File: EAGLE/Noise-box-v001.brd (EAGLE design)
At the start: 160 x 100 mm, 29 parts, among them J1 AVR_SPI_PROG_3X22X3_LOCK, J2 BATT, J4 MICRO-SD_CARD_SOCKET, J5 AUDIO_JACK_3.5MM_SMD, U1 ATMEGA328P_TQFP, U2 MIC5219 3.3V, U3 MCP73831, Y1 12.288MHz

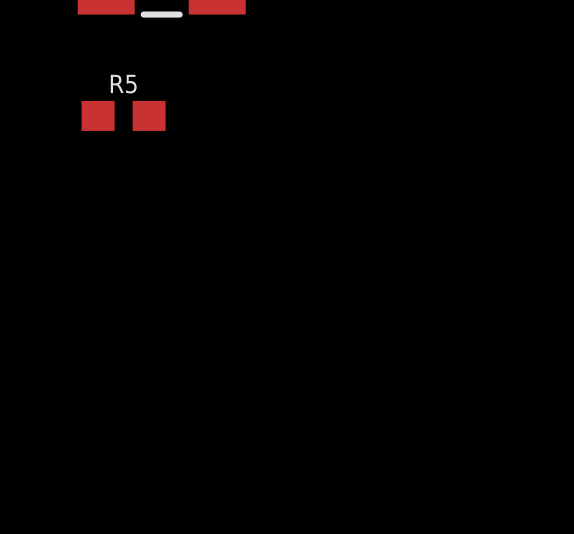
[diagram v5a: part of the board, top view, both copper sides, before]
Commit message: clk
Added crystal for vs1063
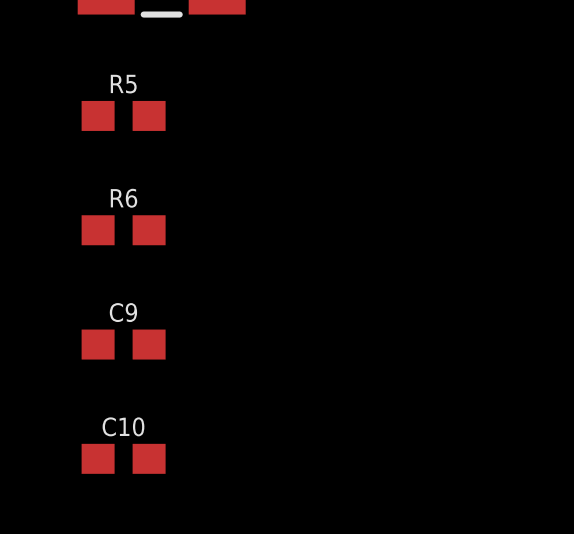
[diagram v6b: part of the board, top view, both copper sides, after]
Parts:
- added C10, C9: 22pF, SparkFun-Capacitors:0603
- added R6: 1M, SparkFun-Resistors:0603
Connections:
- new net N$10: U$3.23
- new net N$11: U$3.13
- new net N$12: U$3.8
- new net N$13: U$3.3
- new net N$14: U$3.32
- new net N$17: C9.2, R6.2, U$3.18, Y1.3
- new net N$18: C10.2, R6.1, U$3.17, Y1.1
- new net N$7: U$3.30
- new net N$8: U$3.29
- new net N$9: U$3.28
- net GND: now also C10.1, C9.1
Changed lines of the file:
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@@
 <attribute name="PROD_ID" value="RES-07828" x="-49.53" y="-134.62" size="1.778" layer="27" display="off"/>
+</element>
+<element name="R6" library="SparkFun-Resistors" package="0603" value="1M" x="-49.53" y="-138.43">
+<attribute name="PROD_ID" value="RES-07868" x="-49.53" y="-138.43" size="1.778" layer="27" display="off"/>
+</element>
+<element name="C9" library="SparkFun-Capacitors" package="0603" value="22pF" x="-49.53" y="-142.24">
+<attribute name="PROD_ID" value="CAP-07876" x="-49.53" y="-142.24" size="1.778" layer="27" display="off"/>
+</element>
+<element name="C10" library="SparkFun-Capacitors" package="0603" value="22pF" x="-49.53" y="-146.05">
+<attribute name="PROD_ID" value="CAP-07876" x="-49.53" y="-146.05" size="1.778" layer="27" display="off"/>
 </element>
 </elements>
@@
 <contactref element="U$3" pad="47"/>
 <contactref element="R5" pad="1"/>
+<contactref element="C9" pad="1"/>
+<contactref element="C10" pad="1"/>
+<wire x1="-50.38" y1="-142.24" x2="-50.38" y2="-146.05" width="0" layer="19" extent="1-1"/>
+<wire x1="-50.38" y1="-134.62" x2="-50.38" y2="-142.24" width="0" layer="19" extent="1-1"/>
 <wire x1="-45.7" y1="-124.9" x2="-50.38" y2="-134.62" width="0" layer="19" extent="1-1"/>
 <wire x1="-48.7" y1="-122.9" x2="-45.7" y2="-124.9" width="0" layer="19" extent="1-1"/>
@@
 <wire x1="-41.7" y1="-124.9" x2="-42.2" y2="-124.9" width="0" layer="19" extent="1-1"/>
 </signal>
+<signal name="N$7">
+<contactref element="U$3" pad="30"/>
+</signal>
+<signal name="N$8">
+<contactref element="U$3" pad="29"/>
+</signal>
+<signal name="N$9">
+<contactref element="U$3" pad="28"/>
+</signal>
+<signal name="N$10">
+<contactref element="U$3" pad="23"/>
+</signal>
+<signal name="N$11">
+<contactref element="U$3" pad="13"/>
+</signal>
+<signal name="N$12">
+<contactref element="U$3" pad="8"/>
+</signal>
+<signal name="N$13">
+<contactref element="U$3" pad="3"/>
+</signal>
+<signal name="N$14">
+<contactref element="U$3" pad="32"/>
+</signal>
+<signal name="N$17">
+<contactref element="U$3" pad="18"/>
+<contactref element="Y1" pad="3"/>
+<contactref element="C9" pad="2"/>
+<contactref element="R6" pad="2"/>
+<wire x1="-48.68" y1="-138.43" x2="-48.68" y2="-142.24" width="0" layer="19" extent="1-1"/>
+<wire x1="-46.41" y1="-128.39" x2="-48.68" y2="-138.43" width="0" layer="19" extent="1-1"/>
+<wire x1="-40.2" y1="-120.9" x2="-46.41" y2="-128.39" width="0" layer="19" extent="1-1"/>
+</signal>
+<signal name="N$18">
+<contactref element="U$3" pad="17"/>
+<contactref element="C10" pad="2"/>
+<contactref element="Y1" pad="1"/>
+<contactref element="R6" pad="1"/>
+<wire x1="-50.38" y1="-138.43" x2="-48.68" y2="-146.05" width="0" layer="19" extent="1-1"/>
+<wire x1="-50.11" y1="-130.69" x2="-50.38" y2="-138.43" width="0" layer="19" extent="1-1"/>
+<wire x1="-40.2" y1="-121.4" x2="-50.11" y2="-130.69" width="0" layer="19" extent="1-1"/>
+</signal>
 </signals>

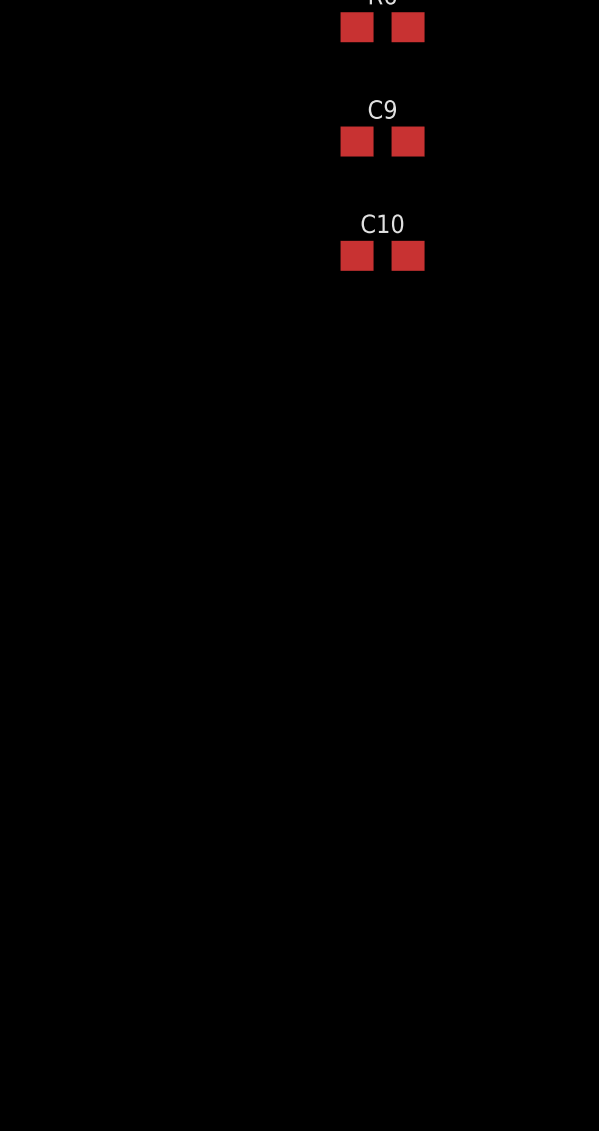
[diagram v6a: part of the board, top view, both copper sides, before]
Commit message: vs1063
Added all support circuitry to vs1063, including extra locations for cap
filtering
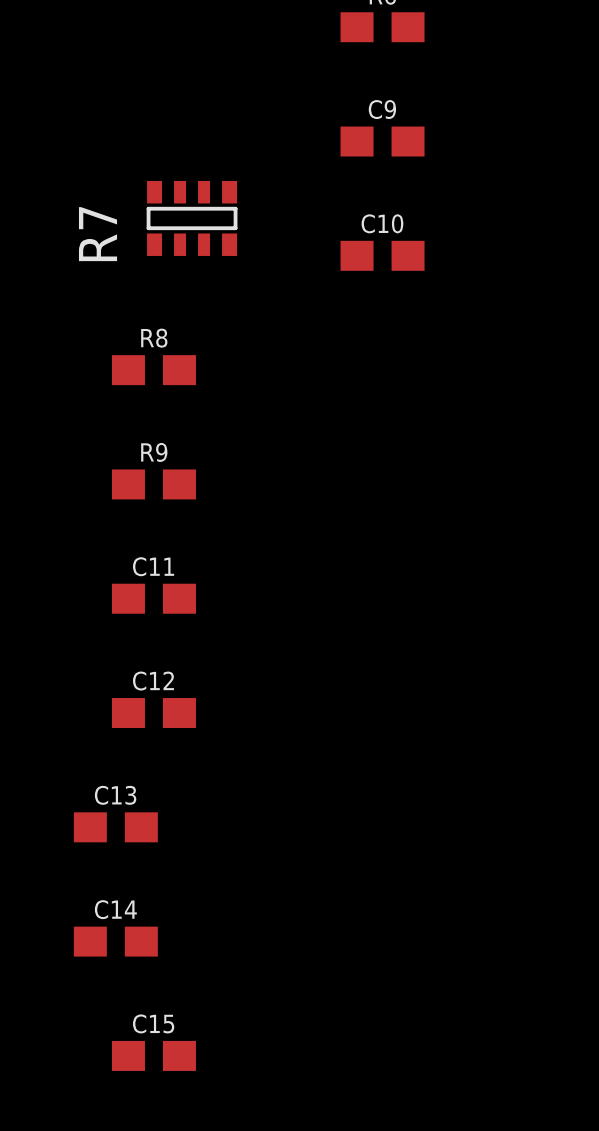
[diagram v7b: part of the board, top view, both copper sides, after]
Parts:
- added C11, C13, C14, C15: 0.1uF, SparkFun-Capacitors:0603
- added C12: 1.0uF, SparkFun-Capacitors:0603
- added R7: RN-4_100K, RJC-2:MNR14
- added R8, R9: 100k, SparkFun-Resistors:0603
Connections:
- net N$10 renamed MP3-CS
- net N$11 renamed MP3-DCS
- net N$12 renamed MP3-DREQ
- removed net N$13: U$3.3
- removed net N$7: U$3.30
- removed net N$8: U$3.29
- removed net N$9: U$3.28
- new net EN-GPIO1: R7.6, U$3.34
- new net GBUF: U$3.42
- new net GPIO0: R7.5, U$3.33
- new net LEFT: U$3.46
- new net MP3-MIDI-RX: R9.1, U$3.26
- new net MP3-RST: R8.1, U$3.3
- new net N$15: R7.7, U$3.36
- new net N$21: C12.1, U$3.44
- new net RIGHT: U$3.39
- net +3V3: now also C11.1, C13.1, C14.1, R8.2, R9.2, U$3.14, U$3.19, U$3.32, U$3.38, U$3.43, U$3.45, U$3.6
- net GND: now also C11.2, C12.2, C13.2, C14.2, C15.2, R7.1, R7.2, R7.3, R7.4
- net MISO: now also U$3.30
- net MOSI: now also U$3.29
- net N$14: now also R7.8, U$3.25; no longer U$3.32
- net SCK: now also U$3.28
- net VCC: now also C15.1, U$3.24, U$3.31, U$3.5, U$3.7
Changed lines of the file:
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@@
 <layer number="230" name="230bmp" color="7" fill="1" visible="yes" active="yes"/>
 <layer number="231" name="231bmp" color="7" fill="1" visible="yes" active="yes"/>
+<layer number="232" name="Eagle3D_PG2" color="7" fill="1" visible="no" active="no"/>
+<layer number="233" name="Eagle3D_PG3" color="7" fill="1" visible="no" active="no"/>
 <layer number="248" name="Housing" color="7" fill="1" visible="yes" active="yes"/>
 <layer number="249" name="Edge" color="7" fill="1" visible="yes" active="yes"/>
@@
 <attribute name="PROD_ID" value="CAP-07876" x="-49.53" y="-146.05" size="1.778" layer="27" display="off"/>
 </element>
+<element name="R7" library="RJC-2" package="MNR14" value="RN-4_100K" x="-55.88" y="-144.78">
+<attribute name="PARTNO" value="MNR14ERAPJ104" x="-55.88" y="-144.78" size="1.778" layer="27" display="off"/>
+</element>
+<element name="R8" library="SparkFun-Resistors" package="0603" value="100k" x="-57.15" y="-149.86">
+<attribute name="PROD_ID" value="RES-07828" x="-57.15" y="-149.86" size="1.778" layer="27" display="off"/>
+</element>
+<element name="R9" library="SparkFun-Resistors" package="0603" value="100k" x="-57.15" y="-153.67">
+<attribute name="PROD_ID" value="RES-07828" x="-57.15" y="-153.67" size="1.778" layer="27" display="off"/>
+</element>
+<element name="C11" library="SparkFun-Capacitors" package="0603" value="0.1uF" x="-57.15" y="-157.48">
+<attribute name="PROD_ID" value="CAP-08604" x="-57.15" y="-157.48" size="1.778" layer="27" display="off"/>
+</element>
+<element name="C12" library="SparkFun-Capacitors" package="0603" value="1.0uF" x="-57.15" y="-161.29">
+<attribute name="PROD_ID" value="CAP-00868" x="-57.15" y="-161.29" size="1.778" layer="27" display="off"/>
+</element>
+<element name="C13" library="SparkFun-Capacitors" package="0603" value="0.1uF" x="-58.42" y="-165.1">
+<attribute name="PROD_ID" value="CAP-08604" x="-57.15" y="-165.1" size="1.778" layer="27" display="off"/>
+</element>
+<element name="C14" library="SparkFun-Capacitors" package="0603" value="0.1uF" x="-58.42" y="-168.91">
+<attribute name="PROD_ID" value="CAP-08604" x="-57.15" y="-168.91" size="1.778" layer="27" display="off"/>
+</element>
+<element name="C15" library="SparkFun-Capacitors" package="0603" value="0.1uF" x="-57.15" y="-172.72">
+<attribute name="PROD_ID" value="CAP-08604" x="-57.15" y="-172.72" size="1.778" layer="27" display="off"/>
+</element>
 </elements>
 <signals>
@@
 <contactref element="U$1" pad="3"/>
 <contactref element="J4" pad="VCC"/>
+<contactref element="U$3" pad="38"/>
+<contactref element="U$3" pad="45"/>
+<contactref element="U$3" pad="43"/>
+<contactref element="U$3" pad="6"/>
+<contactref element="U$3" pad="19"/>
+<contactref element="U$3" pad="14"/>
+<contactref element="U$3" pad="32"/>
+<contactref element="R9" pad="2"/>
+<contactref element="R8" pad="2"/>
+<contactref element="C11" pad="1"/>
+<contactref element="C13" pad="1"/>
+<contactref element="C14" pad="1"/>
+<wire x1="-59.27" y1="-165.1" x2="-59.27" y2="-168.91" width="0" layer="19" extent="1-1"/>
+<wire x1="-58" y1="-157.48" x2="-59.27" y2="-165.1" width="0" layer="19" extent="1-1"/>
+<wire x1="-56.3" y1="-153.67" x2="-58" y2="-157.48" width="0" layer="19" extent="1-1"/>
+<wire x1="-56.3" y1="-149.86" x2="-56.3" y2="-153.67" width="0" layer="19" extent="1-1"/>
+<wire x1="-44.7" y1="-124.9" x2="-56.3" y2="-149.86" width="0" layer="19" extent="1-1"/>
+<wire x1="-40.2" y1="-122.9" x2="-44.7" y2="-124.9" width="0" layer="19" extent="1-1"/>
+<wire x1="-40.2" y1="-120.4" x2="-40.2" y2="-122.9" width="0" layer="19" extent="1-1"/>
+<wire x1="-48.7" y1="-121.9" x2="-44.7" y2="-124.9" width="0" layer="19" extent="1-1"/>
+<wire x1="-48.7" y1="-120.9" x2="-48.7" y2="-121.9" width="0" layer="19" extent="1-1"/>
+<wire x1="-48.7" y1="-118.4" x2="-48.7" y2="-120.9" width="0" layer="19" extent="1-1"/>
+<wire x1="-45.2" y1="-116.4" x2="-48.7" y2="-118.4" width="0" layer="19" extent="1-1"/>
+<wire x1="-27.23" y1="-93.24" x2="-45.2" y2="-116.4" width="0" layer="19" extent="1-1"/>
 <wire x1="-32.37" y1="-71.945" x2="-27.23" y2="-93.24" width="0" layer="19" extent="1-1"/>
 <wire x1="-33.67" y1="-71.945" x2="-32.37" y2="-71.945" width="0" layer="19" extent="1-1"/>
@@
 <contactref element="C9" pad="1"/>
 <contactref element="C10" pad="1"/>
+<contactref element="R7" pad="1"/>
+<contactref element="R7" pad="2"/>
+<contactref element="R7" pad="3"/>
+<contactref element="R7" pad="4"/>
+<contactref element="C12" pad="2"/>
+<contactref element="C11" pad="2"/>
+<contactref element="C13" pad="2"/>
+<contactref element="C14" pad="2"/>
+<contactref element="C15" pad="2"/>
+<wire x1="-57.57" y1="-168.91" x2="-56.3" y2="-172.72" width="0" layer="19" extent="1-1"/>
+<wire x1="-57.57" y1="-165.1" x2="-57.57" y2="-168.91" width="0" layer="19" extent="1-1"/>
+<wire x1="-56.3" y1="-161.29" x2="-57.57" y2="-165.1" width="0" layer="19" extent="1-1"/>
+<wire x1="-56.3" y1="-157.48" x2="-56.3" y2="-161.29" width="0" layer="19" extent="1-1"/>
+<wire x1="-56.28" y1="-145.68" x2="-56.3" y2="-157.48" width="0" layer="19" extent="1-1"/>
+<wire x1="-55.48" y1="-145.68" x2="-56.28" y2="-145.68" width="0" layer="19" extent="1-1"/>
+<wire x1="-57.13" y1="-145.68" x2="-56.28" y2="-145.68" width="0" layer="19" extent="1-1"/>
+<wire x1="-54.63" y1="-145.68" x2="-55.48" y2="-145.68" width="0" layer="19" extent="1-1"/>
+<wire x1="-50.38" y1="-146.05" x2="-54.63" y2="-145.68" width="0" layer="19" extent="1-1"/>
 <wire x1="-50.38" y1="-142.24" x2="-50.38" y2="-146.05" width="0" layer="19" extent="1-1"/>
 <wire x1="-50.38" y1="-134.62" x2="-50.38" y2="-142.24" width="0" layer="19" extent="1-1"/>
@@
 <contactref element="J1" pad="4"/>
 <contactref element="J4" pad="DI"/>
+<contactref element="U$3" pad="29"/>
+<wire x1="-28.33" y1="-93.44" x2="-43.7" y2="-116.4" width="0" layer="19" extent="1-1"/>
 <wire x1="-5.08" y1="-2.667" x2="-28.33" y2="-93.44" width="0" layer="19" extent="1-1"/>
 </signal>
@@
 <contactref element="J1" pad="3"/>
 <contactref element="J4" pad="SCLK"/>
+<contactref element="U$3" pad="28"/>
+<wire x1="-26.13" y1="-93.44" x2="-43.2" y2="-116.4" width="0" layer="19" extent="1-1"/>
 <wire x1="-5.08" y1="-5.207" x2="-26.13" y2="-93.44" width="0" layer="19" extent="1-1"/>
 </signal>
@@
 <contactref element="J1" pad="1"/>
 <contactref element="J4" pad="DO"/>
+<contactref element="U$3" pad="30"/>
+<wire x1="-23.93" y1="-93.44" x2="-44.2" y2="-116.4" width="0" layer="19" extent="1-1"/>
 <wire x1="-7.62" y1="-4.953" x2="-23.93" y2="-93.44" width="0" layer="19" extent="1-1"/>
 </signal>
@@
 <contactref element="C7" pad="+"/>
 <contactref element="C8" pad="1"/>
+<contactref element="U$3" pad="5"/>
+<contactref element="U$3" pad="31"/>
+<contactref element="U$3" pad="7"/>
+<contactref element="U$3" pad="24"/>
+<contactref element="C15" pad="1"/>
+<wire x1="-45.2" y1="-124.9" x2="-58" y2="-172.72" width="0" layer="19" extent="1-1"/>
+<wire x1="-44.2" y1="-124.9" x2="-45.2" y2="-124.9" width="0" layer="19" extent="1-1"/>
+<wire x1="-40.2" y1="-117.9" x2="-44.2" y2="-124.9" width="0" layer="19" extent="1-1"/>
+<wire x1="-44.7" y1="-116.4" x2="-40.2" y2="-117.9" width="0" layer="19" extent="1-1"/>
+<wire x1="-33.87" y1="-80.01" x2="-44.7" y2="-116.4" width="0" layer="19" extent="1-1"/>
 <wire x1="-31.62" y1="-76.2" x2="-33.87" y2="-80.01" width="0" layer="19" extent="1-1"/>
 <wire x1="-33.67" y1="-70.295" x2="-31.62" y2="-76.2" width="0" layer="19" extent="1-1"/>
@@
 <wire x1="-41.7" y1="-124.9" x2="-42.2" y2="-124.9" width="0" layer="19" extent="1-1"/>
 </signal>
-<signal name="N$7">
-<contactref element="U$3" pad="30"/>
-</signal>
-<signal name="N$8">
-<contactref element="U$3" pad="29"/>
-</signal>
-<signal name="N$9">
-<contactref element="U$3" pad="28"/>
-</signal>
-<signal name="N$10">
+<signal name="MP3-CS">
 <contactref element="U$3" pad="23"/>
 </signal>
-<signal name="N$11">
+<signal name="MP3-DCS">
 <contactref element="U$3" pad="13"/>
 </signal>
-<signal name="N$12">
+<signal name="MP3-DREQ">
 <contactref element="U$3" pad="8"/>
 </signal>
-<signal name="N$13">
+<signal name="MP3-RST">
 <contactref element="U$3" pad="3"/>
-</signal>
-<signal name="N$14">
-<contactref element="U$3" pad="32"/>
+<contactref element="R8" pad="1"/>
+<wire x1="-46.2" y1="-124.9" x2="-58" y2="-149.86" width="0" layer="19" extent="1-1"/>
 </signal>
 <signal name="N$17">
@@
 <wire x1="-40.2" y1="-121.4" x2="-50.11" y2="-130.69" width="0" layer="19" extent="1-1"/>
 </signal>
+<signal name="N$14">
+<contactref element="U$3" pad="25"/>
+<contactref element="R7" pad="8"/>
+<wire x1="-41.7" y1="-116.4" x2="-57.13" y2="-143.93" width="0" layer="19" extent="1-1"/>
+</signal>
+<signal name="N$15">
+<contactref element="U$3" pad="36"/>
+<contactref element="R7" pad="7"/>
+<wire x1="-47.2" y1="-116.4" x2="-56.28" y2="-143.93" width="0" layer="19" extent="1-1"/>
+</signal>
+<signal name="EN-GPIO1">
+<contactref element="U$3" pad="34"/>
+<contactref element="R7" pad="6"/>
+<wire x1="-46.2" y1="-116.4" x2="-55.48" y2="-143.93" width="0" layer="19" extent="1-1"/>
+</signal>
+<signal name="GPIO0">
+<contactref element="U$3" pad="33"/>
+<contactref element="R7" pad="5"/>
+<wire x1="-45.7" y1="-116.4" x2="-54.63" y2="-143.93" width="0" layer="19" extent="1-1"/>
+</signal>
+<signal name="GBUF">
+<contactref element="U$3" pad="42"/>
+</signal>
+<signal name="RIGHT">
+<contactref element="U$3" pad="39"/>
+</signal>
+<signal name="LEFT">
+<contactref element="U$3" pad="46"/>
+</signal>
+<signal name="N$21">
+<contactref element="U$3" pad="44"/>
+<contactref element="C12" pad="1"/>
+<wire x1="-48.7" y1="-121.4" x2="-58" y2="-161.29" width="0" layer="19" extent="1-1"/>
+</signal>
+<signal name="MP3-MIDI-RX">
+<contactref element="U$3" pad="26"/>
+<contactref element="R9" pad="1"/>
+<wire x1="-42.2" y1="-116.4" x2="-58" y2="-153.67" width="0" layer="19" extent="1-1"/>
+</signal>
 </signals>

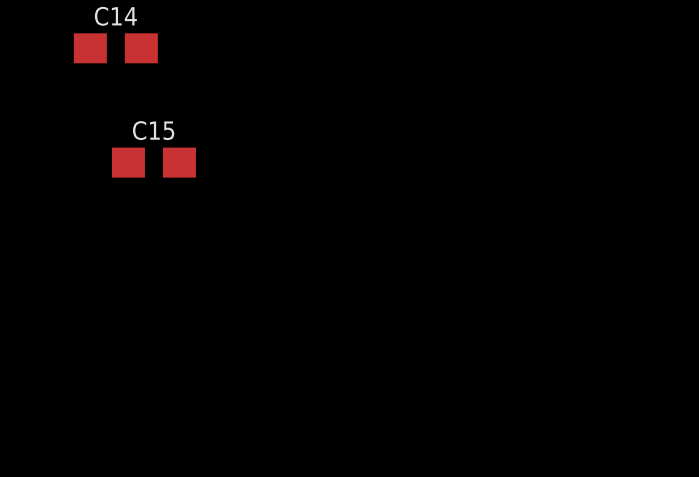
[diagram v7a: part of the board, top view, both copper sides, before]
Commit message: Audio amp
Added simple audio amplifier
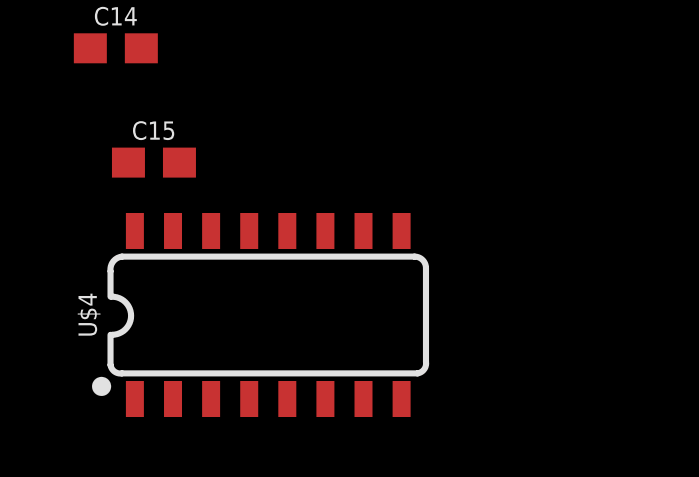
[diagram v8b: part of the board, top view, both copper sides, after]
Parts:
- added U$4: (no value), RJC:SO16
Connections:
- net GND: now also U$4.12, U$4.13, U$4.6
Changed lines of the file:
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@@
 <attribute name="PROD_ID" value="CAP-08604" x="-57.15" y="-172.72" size="1.778" layer="27" display="off"/>
+</element>
+<element name="U$4" library="RJC" package="SO16" value="" x="-53.34" y="-177.8">
+<attribute name="PARTNO" value="PAM8407" x="-53.34" y="-177.8" size="1.778" layer="27" display="off"/>
 </element>
 </elements>
@@
 <contactref element="C14" pad="2"/>
 <contactref element="C15" pad="2"/>
+<contactref element="U$4" pad="13"/>
+<contactref element="U$4" pad="6"/>
+<contactref element="U$4" pad="12"/>
+<wire x1="-52.705" y1="-175" x2="-51.435" y2="-180.6" width="0" layer="19" extent="1-1"/>
+<wire x1="-53.975" y1="-175" x2="-52.705" y2="-175" width="0" layer="19" extent="1-1"/>
+<wire x1="-56.3" y1="-172.72" x2="-53.975" y2="-175" width="0" layer="19" extent="1-1"/>
 <wire x1="-57.57" y1="-168.91" x2="-56.3" y2="-172.72" width="0" layer="19" extent="1-1"/>
 <wire x1="-57.57" y1="-165.1" x2="-57.57" y2="-168.91" width="0" layer="19" extent="1-1"/>
